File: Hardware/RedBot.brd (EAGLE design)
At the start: 94 x 49.5 mm, 66 parts, among them U1 ATMEGA328P, U2 TB6612FNG, U3 MIC5219 5V, U4 MIC5219 3.3V, U5 FT232RLSSOP, U6 7408SE, Y1 16MHz

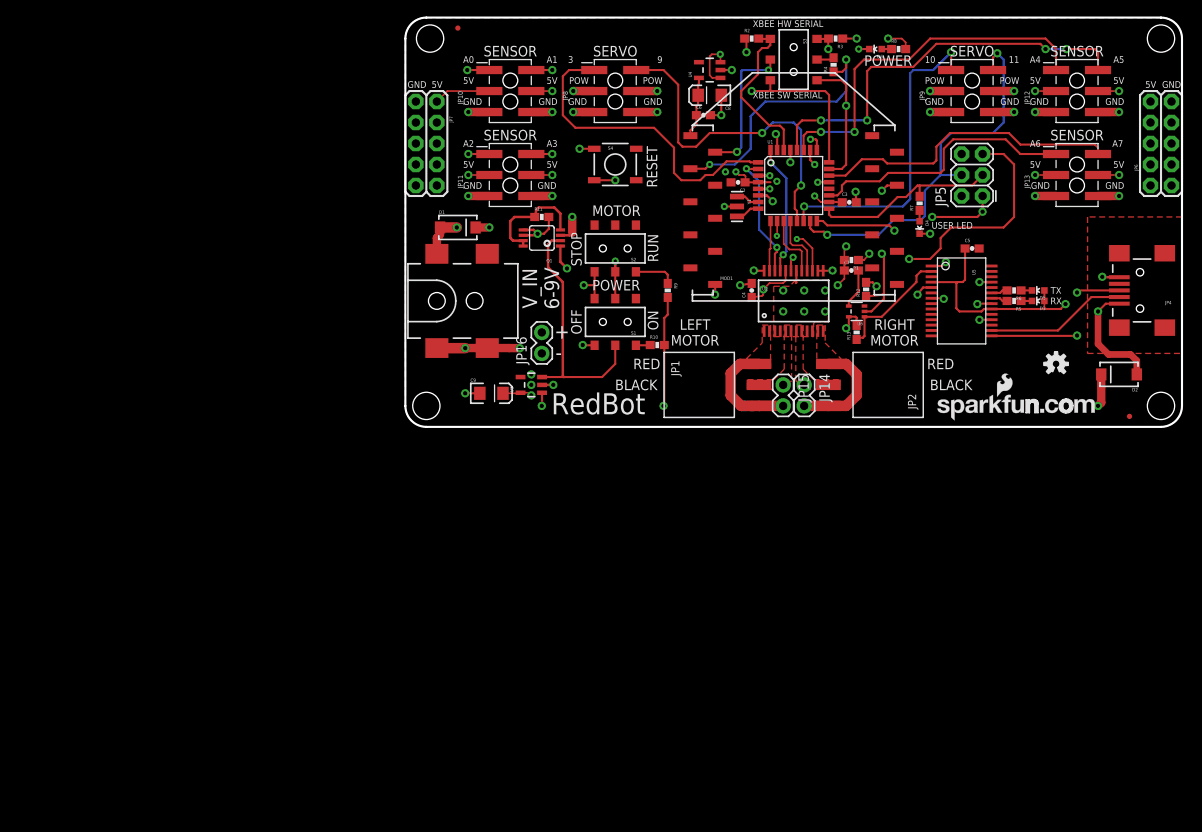
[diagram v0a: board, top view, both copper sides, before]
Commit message: First pass at converting schematic
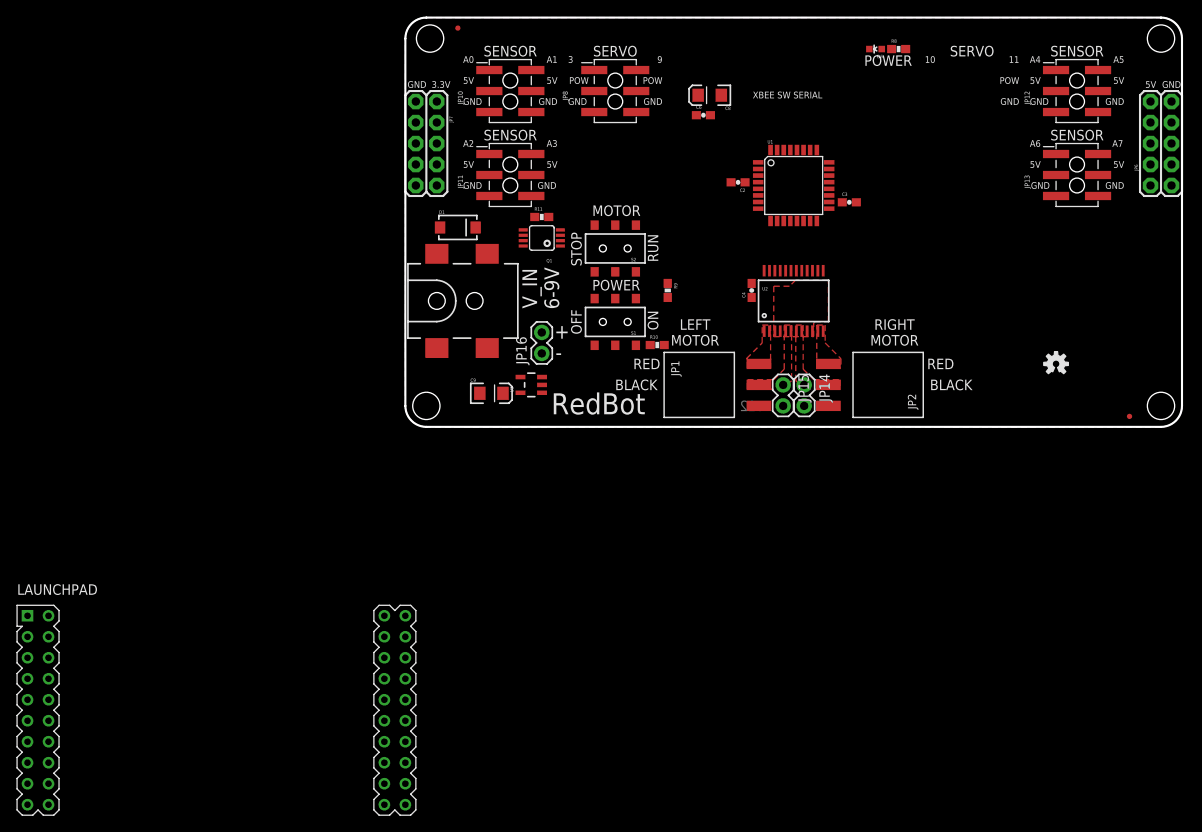
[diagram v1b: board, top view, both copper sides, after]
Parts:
- removed C5, C7: 0.1uF, SparkFun-Capacitors:0603-CAP
- removed D2: (no value), SparkFun-DiscreteSemi:SMA-DIODE
- removed D3, D4, D5: GREEN, SparkFun-LED:LED-0603
- removed JP4: USB-B, SparkFun-Connectors:USB-MINIB
- removed JP5: AVR_SPI_PRG_6PTH, SparkFun-Connectors:2X3
- removed JP9: (no value), SparkFun-Connectors:2X3_SMT_POSTS
- removed MOD1: XBEE-1B3, SparkFun-RF:XBEE-SMD
- removed R1, R12, R13: 10k, SparkFun-Resistors:0603-RES
- removed R2, R3, R4, R5, R6, R7: 1k, SparkFun-Resistors:0603-RES
- removed S3: DPDT, SparkFun-Electromechanical:AYZ0202
- removed S4: (no value), SparkFun-Electromechanical:TACTILE_SWITCH_SMD
- removed SFE-LOGO1: LOGO-SFENEW, SparkFun-Aesthetics:SFE-NEW-WEBLOGO
- removed U$21: FOUR_LAYER_WARNING, SparkFun-Aesthetics:FOUR_LAYER_WARNING
- removed U4: MIC5219 3.3V, SparkFun-PowerIC:SOT23-5
- removed U5: FT232RLSSOP, SparkFun-DigitalIC:SSOP28DB
- removed U6: 7408SE, SparkFun-DigitalIC:SOT353
- removed Y1: 16MHz, SparkFun-FreqCtrl:RESONATOR-SMD
- added LAUNCHPAD: BOOSTERPACK, zlalanne:BOOSTERPACK40
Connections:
- removed net AREF: U1.20
- removed net FT232_RXI: R3.1, U5.5
- removed net FT232_TXO: R2.1, U5.1
- removed net FTDI_DTR: R13.1, U5.2, U6.1
- removed net N$1: R4.2, S3.2
- removed net N$23: U1.8, Y1.3
- removed net N$24: U1.7, Y1.1
- removed net N$26: JP4.D-, U5.16
- removed net N$27: JP4.D+, U5.15
- removed net N$3: D5.C, R6.1
- removed net N$4: D3.C, R5.1
- removed net N$5: C7.2, U6.4
- removed net N$6: JP4.MTN1, JP4.MTN2, JP4.MTN3, JP4.MTN4
- removed net N$7: D4.A, R7.1
- removed net RESET: C7.1, JP5.5, R1.2, S4.3, U1.29
- removed net RXI: R2.2, S3.4, U1.30
- removed net RXLED: R5.2, U5.22
- removed net SENSOR_0/SW_TXO: JP10.1, S3.3, U1.23
- removed net SENSOR_1/SW_RXI: JP10.2, S3.6, U1.24
- removed net SERVO_3: JP9.1, U1.14
- removed net TXLED: R6.2, U5.23
- removed net TXO: R3.2, S3.1, U1.31
- removed net V_USB: C5.1, D2.A, D3.A, D5.A, JP4.VBUS, U5.20, U5.4
- removed net XBEE_DIO3: MOD1.17, R12.1, U6.2
- removed net XBEE_RXI: MOD1.3, R4.1
- removed net XBEE_TXO: MOD1.2, S3.5
- new net PWM_L: LAUNCHPAD.40
- new net PWM_R: LAUNCHPAD.39
- new net SENSOR_0: JP10.1, LAUNCHPAD.23
- new net SENSOR_1: JP10.2, LAUNCHPAD.24
- net 3.3V: now also JP10.3, JP10.4, JP11.3, JP11.4, JP12.3, JP12.4, JP13.3, JP13.4, JP7.1, JP7.3, JP7.5, JP7.7, JP7.9, LAUNCHPAD.1; no longer MOD1.1, U4.5
- net 5V: now also LAUNCHPAD.21; no longer JP10.3, JP10.4, JP11.3, JP11.4, JP12.3, JP12.4, JP13.3, JP13.4, JP5.2, JP7.1, JP7.3, JP7.5, JP7.7, JP7.9, R1.1, R12.2, R13.2, U1.18, U1.4, U1.6, U4.1, U4.3, U6.5
- net GND: now also LAUNCHPAD.20, LAUNCHPAD.22; no longer C5.2, D4.C, JP4.GND, JP5.6, JP9.5, JP9.6, MOD1.10, S4.1, U1.21, U1.3, U1.5, U4.2, U5.18, U5.21, U5.25, U5.26, U5.7, U6.3, Y1.2
- net L_CTRL_1: now also LAUNCHPAD.34; no longer U1.32
- net L_CTRL_2: now also LAUNCHPAD.33
- net MISO: no longer JP5.1
- net PWML: no longer U1.9
- net PWMR: no longer U1.10
- net R_CTRL_1: now also LAUNCHPAD.32; no longer U1.11
- net R_CTRL_2: now also LAUNCHPAD.31; no longer U1.12
- net SCK: no longer JP5.3, R7.2
- net SENSOR_2: now also LAUNCHPAD.25; no longer U1.25
- net SENSOR_3: now also LAUNCHPAD.26; no longer U1.26
- net SENSOR_4: now also LAUNCHPAD.27; no longer U1.27
- net SENSOR_5: now also LAUNCHPAD.28; no longer U1.28
- net SENSOR_6: now also LAUNCHPAD.2; no longer U1.19
- net SENSOR_7: now also LAUNCHPAD.6; no longer U1.22
- net SERVO_1: now also LAUNCHPAD.38
- net SERVO_2: now also LAUNCHPAD.37
- net SERVO_4/MOSI: no longer JP5.4, JP9.2
- net V_GATED: no longer JP9.3, JP9.4
- net V_IN: no longer D2.C
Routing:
- net RESET: track 84.7 -> 0.00 mm, vias 5 -> 0
- net GND: track 82.2 -> 0.00 mm, vias 43 -> 0
- net SENSOR_0/SW_TXO: track 69.5 -> 0.00 mm, vias 2 -> 0
- net 5V: track 61.4 -> 0.00 mm, vias 20 -> 0
- net SENSOR_0: track 0.00 -> 51.1 mm
- net FT232_TXO: track 50.4 -> 0.00 mm, vias 2 -> 0
- net SENSOR_5: track 49.6 -> 0.00 mm, vias 4 -> 0
- net SENSOR_1/SW_RXI: track 47.8 -> 0.00 mm, vias 2 -> 0
- net SERVO_4/MOSI: track 47.7 -> 0.00 mm, vias 2 -> 0
- net V_USB: track 45.6 -> 0.00 mm, vias 2 -> 0
- net SENSOR_4: track 44.7 -> 0.00 mm, vias 2 -> 0
- net FT232_RXI: track 42.5 -> 0.00 mm, vias 2 -> 0
- net SERVO_2: track 40.9 -> 0.00 mm, vias 2 -> 0
- net SERVO_1: track 38.5 -> 0.00 mm
- net SERVO_3: track 38.4 -> 0.00 mm, vias 2 -> 0
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- removed copper zone on layer 1, net N$6
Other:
- board text added: "3.3V"
- board text removed: "RESET"
- board text removed: "RX"
- board text removed: "TX"
- board text removed: "USER LED"
- board text removed: "XBEE HW SERIAL"
